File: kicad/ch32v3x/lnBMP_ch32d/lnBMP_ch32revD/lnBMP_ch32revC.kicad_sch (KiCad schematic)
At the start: 24 parts, among them J1 BMP Debug1, J2 BMP Debug2, J3 Debug port, J4 USB_OTG, U1 CH32V303RCT6, U2 LM1117-3.3, Y1 Crystal

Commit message: new rev of ch32 pcb
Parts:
- added DFU: SWDFU, Button_Switch_SMD:SW_SPST_CK_RS282G05A3, symbol Switch:SW_DIP_x01
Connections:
- net GND: now also DFU.2

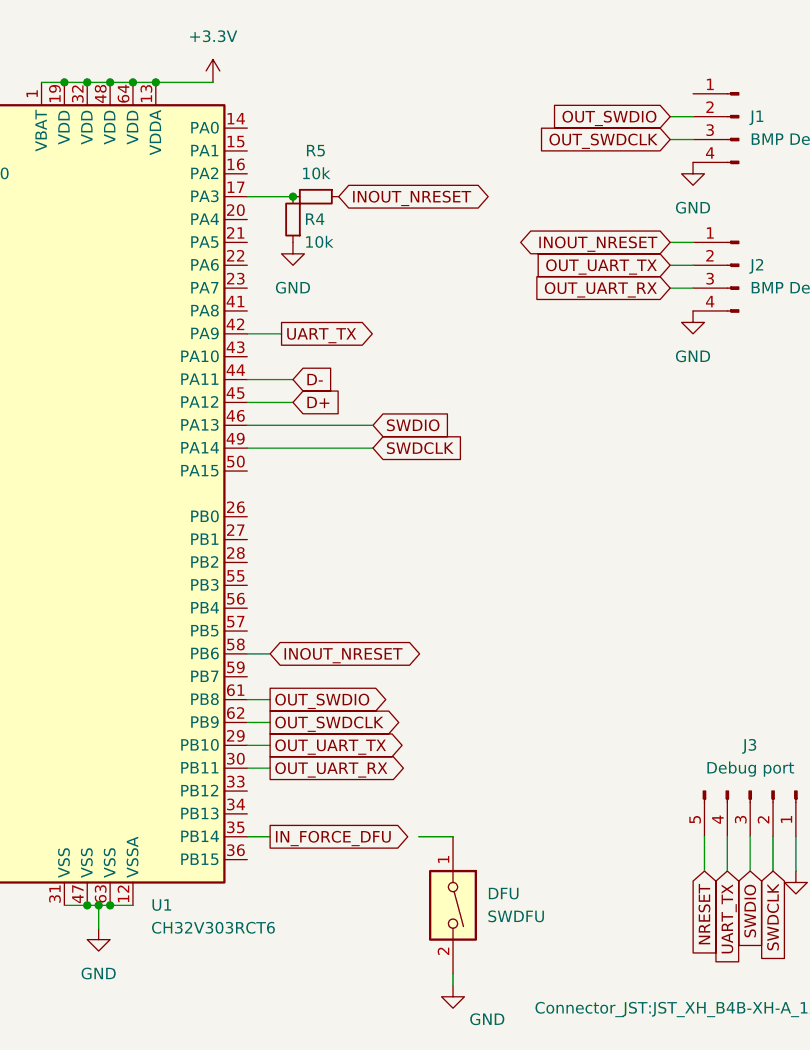
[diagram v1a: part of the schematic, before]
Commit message: pcb/ch32: reduce R5
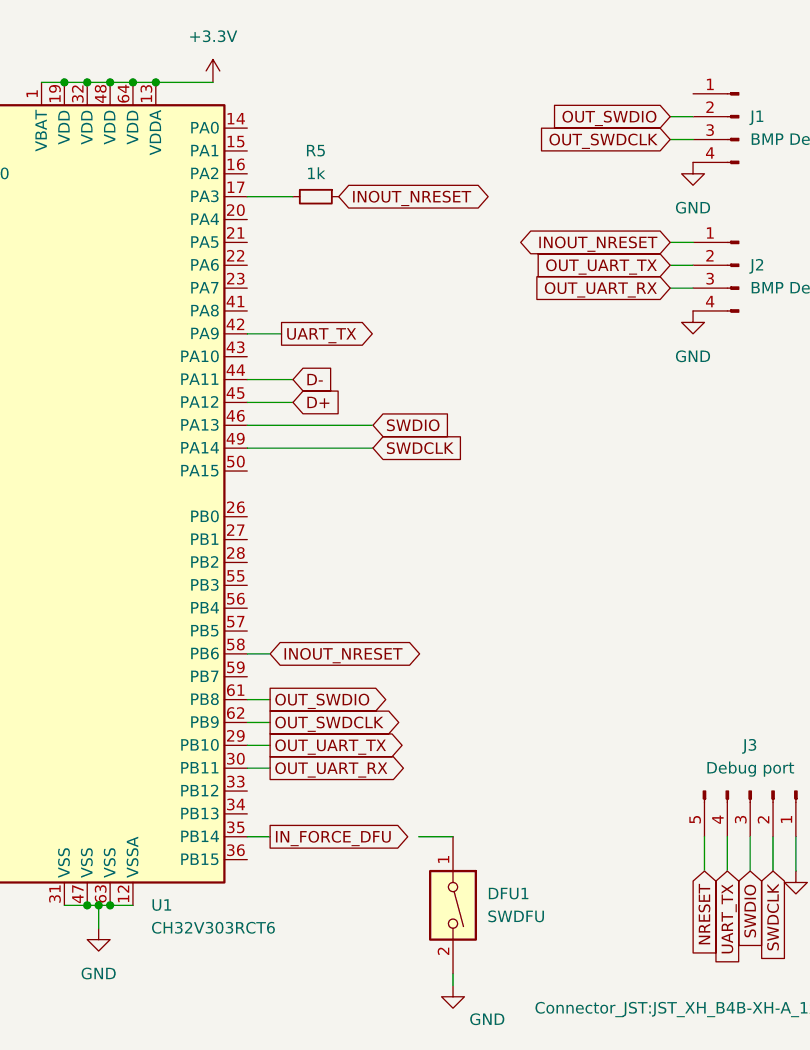
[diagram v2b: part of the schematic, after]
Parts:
- removed R4: 10k, Resistor_SMD:R_0603_1608Metric, symbol Device:R_Small
- R5: value 10k -> 1k
- renumbered DFU to DFU1

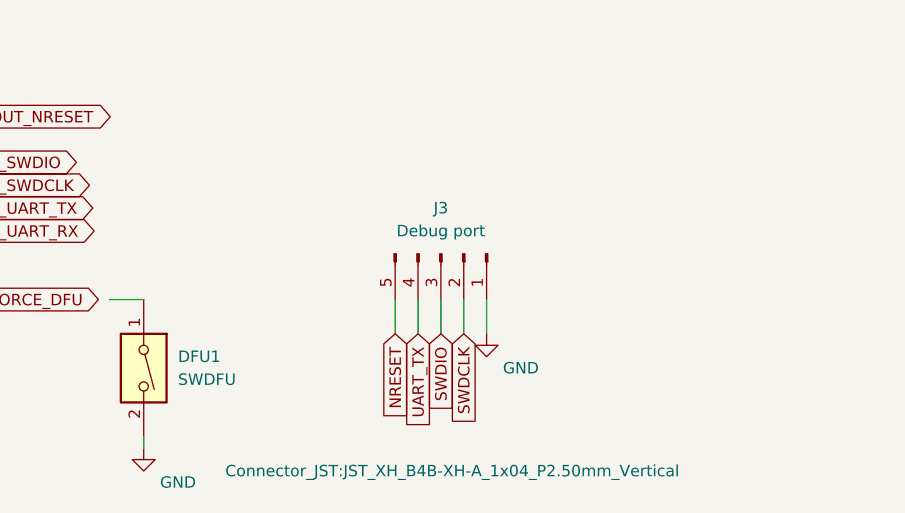
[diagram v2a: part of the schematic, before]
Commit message: kicad/ch32: Fix swapped labels, orienttion
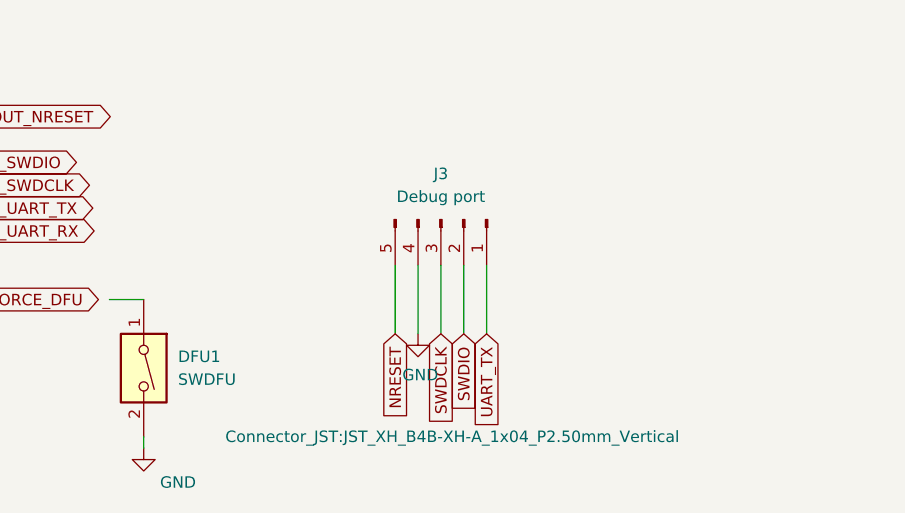
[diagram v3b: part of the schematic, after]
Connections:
- net GND: now also J3.4 (Pin_4); no longer J3.1 (Pin_1)
- net SWDCLK: now also J3.3 (Pin_3); no longer J3.2 (Pin_2)
- net SWDIO: now also J3.2 (Pin_2); no longer J3.3 (Pin_3)
- net UART_TX: now also J3.1 (Pin_1); no longer J3.4 (Pin_4)
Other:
- moved on the sheet: J3
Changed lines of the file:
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@@
     (stroke (width 0) (type default))
   )
-  (wire (pts (xy 142.24 146.05) (xy 142.24 149.86))
+  (wire (pts (xy 142.24 142.24) (xy 142.24 149.86))
     (stroke (width 0) (type default))
   )
@@
     (stroke (width 0) (type default))
   )
-  (wire (pts (xy 144.78 146.05) (xy 144.78 149.86))
+  (wire (pts (xy 144.78 142.24) (xy 144.78 149.86))
     (stroke (width 0) (type default))
   )
@@
     (stroke (width 0) (type default))
   )
-  (wire (pts (xy 139.7 146.05) (xy 139.7 149.86))
+  (wire (pts (xy 139.7 142.24) (xy 139.7 149.86))
     (stroke (width 0) (type default))
   )
@@
     (stroke (width 0) (type default))
   )
-  (wire (pts (xy 147.32 146.05) (xy 147.32 149.86))
+  (wire (pts (xy 147.32 142.24) (xy 147.32 149.86))
     (stroke (width 0) (type default))
   )
@@
     (stroke (width 0) (type default))
   )
-  (wire (pts (xy 137.16 146.05) (xy 137.16 149.86))
+  (wire (pts (xy 137.16 142.24) (xy 137.16 149.86))
     (stroke (width 0) (type default))
   )
@@
     )
   )
-  (global_label "UART_TX" (shape input) (at 139.7 149.86 270) (fields_autoplaced)
+  (global_label "UART_TX" (shape input) (at 147.32 149.86 270) (fields_autoplaced)
     (effects (font (size 1.27 1.27)) (justify right))
-    (property "Intersheetrefs" "${INTERSHEET_REFS}" (at 139.7 160.5672 90)
+    (property "Intersheetrefs" "${INTERSHEET_REFS}" (at 147.32 160.5672 90)
       (effects (font (size 1.27 1.27)) (justify right) hide)
     )
@@
     )
   )
-  (global_label "SWDCLK" (shape input) (at 144.78 149.86 270) (fields_autoplaced)
+  (global_label "SWDCLK" (shape input) (at 142.24 149.86 270) (fields_autoplaced)
     (effects (font (size 1.27 1.27)) (justify right))
-    (property "Intersheetrefs" "${INTERSHEET_REFS}" (at 144.8594 159.7721 90)
-      (effects (font (size 1.27 1.27)) (justify left) hide)
-    )
-  )
-  (global_label "SWDIO" (shape input) (at 142.24 149.86 270) (fields_autoplaced)
+    (property "Intersheetrefs" "${INTERSHEET_REFS}" (at 142.3194 159.7721 90)
+      (effects (font (size 1.27 1.27)) (justify left) hide)
+    )
+  )
+  (global_label "SWDIO" (shape input) (at 144.78 149.86 270) (fields_autoplaced)
     (effects (font (size 1.27 1.27)) (justify right))
-    (property "Intersheetrefs" "${INTERSHEET_REFS}" (at 142.3194 158.1393 90)
+    (property "Intersheetrefs" "${INTERSHEET_REFS}" (at 144.8594 158.1393 90)
       (effects (font (size 1.27 1.27)) (justify left) hide)
     )
@@
     )
   )
-  (symbol (lib_id "Connector:Conn_01x05_Male") (at 142.24 140.97 270) (unit 1)
+  (symbol (lib_id "Connector:Conn_01x05_Male") (at 142.24 137.16 270) (unit 1)
     (exclude_from_sim no) (in_bom yes) (on_board yes) (dnp no)
-    (property "Reference" "J3" (at 142.24 135.89 90)
-      (effects (font (size 1.27 1.27)))
-    )
-    (property "Value" "Debug port" (at 142.24 138.43 90)
-      (effects (font (size 1.27 1.27)))
-    )
-    (property "Footprint" "Connector_JST:JST_XH_B4B-XH-A_1x04_P2.50mm_Vertical" (at 143.51 165.1 90)
-      (effects (font (size 1.27 1.27)))
-    )
-    (property "Datasheet" "~" (at 142.24 140.97 0)
-      (effects (font (size 1.27 1.27)) hide)
-    )
-    (property "Description" "" (at 142.24 140.97 0)
+    (property "Reference" "J3" (at 142.24 132.08 90)
+      (effects (font (size 1.27 1.27)))
+    )
+    (property "Value" "Debug port" (at 142.24 134.62 90)
+      (effects (font (size 1.27 1.27)))
+    )
+    (property "Footprint" "Connector_JST:JST_XH_B4B-XH-A_1x04_P2.50mm_Vertical" (at 143.51 161.29 90)
+      (effects (font (size 1.27 1.27)))
+    )
+    (property "Datasheet" "~" (at 142.24 137.16 0)
+      (effects (font (size 1.27 1.27)) hide)
+    )
+    (property "Description" "" (at 142.24 137.16 0)
       (effects (font (size 1.27 1.27)) hide)
     )
@@
     )
   )
-  (symbol (lib_id "power:GND") (at 147.32 149.86 0) (unit 1)
+  (symbol (lib_id "power:GND") (at 139.7 149.86 0) (unit 1)
     (exclude_from_sim no) (in_bom yes) (on_board yes) (dnp no)
-    (property "Reference" "#PWR012" (at 147.32 156.21 0)
-      (effects (font (size 1.27 1.27)) hide)
-    )
-    (property "Value" "GND" (at 151.13 153.67 0)
-      (effects (font (size 1.27 1.27)))
-    )
-    (property "Footprint" "" (at 147.32 149.86 0)
-      (effects (font (size 1.27 1.27)) hide)
-    )
-    (property "Datasheet" "" (at 147.32 149.86 0)
-      (effects (font (size 1.27 1.27)) hide)
-    )
-    (property "Description" "" (at 147.32 149.86 0)
-      (effects (font (size 1.27 1.27)) hide)
-    )
+    (property "Reference" "#PWR012" (at 139.7 156.21 0)
+      (effects (font (size 1.27 1.27)) hide)
+    )
+    (property "Value" "GND" (at 139.954 154.432 0)
+      (effects (font (size 1.27 1.27)))
+    )
+    (property "Footprint" "" (at 139.7 149.86 0)
+      (effects (font (size 1.27 1.27)) hide)
+    )
+    (property "Datasheet" "" (at 139.7 149.86 0)
+      (effects (font (size 1.27 1.27)) hide)
+    )
+    (property "Description" "" (at 139.7 149.86 0)
+      (effects (font (size 1.27 1.27)) hide)
+    )
